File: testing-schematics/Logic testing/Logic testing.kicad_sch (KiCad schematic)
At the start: 14 parts, among them J1 Fencer's Wire, J2 Opponent's Wire, K1 G6K-2, K2 G6K-2, K3 G6K-2, Q1 BC547, Q2 BC547, Q3 BC547

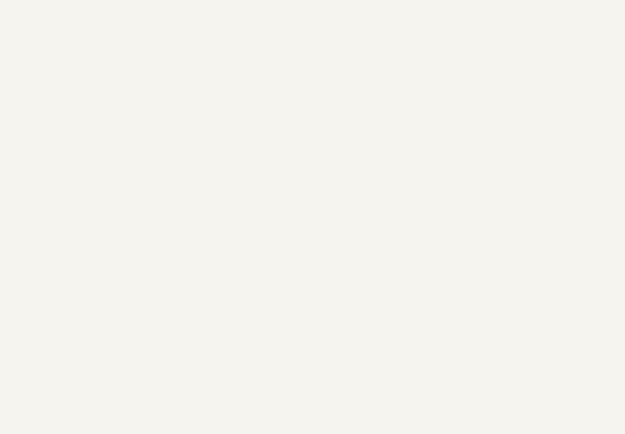
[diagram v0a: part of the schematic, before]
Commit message: Add voltage divider schematics and journal entry;
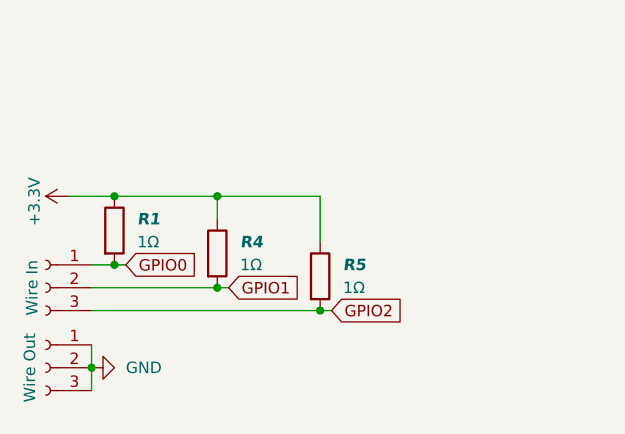
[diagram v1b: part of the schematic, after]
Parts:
- added J3: Wire In, symbol Connector:Conn_01x03_Socket
- added J4: Wire Out, symbol Connector:Conn_01x03_Socket
- added R1, R4, R5: 1Ω, symbol Device:R
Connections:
- net +3.3V: now also R1.1, R4.1, R5.1
- net GND: now also J4.1 (Pin_1), J4.2 (Pin_2), J4.3 (Pin_3)
- net GPIO1: now also J3.2 (Pin_2), R4.2
- net GPIO2: now also J3.3 (Pin_3), R5.2
- new net GPIO0: J3.1 (Pin_1), R1.2

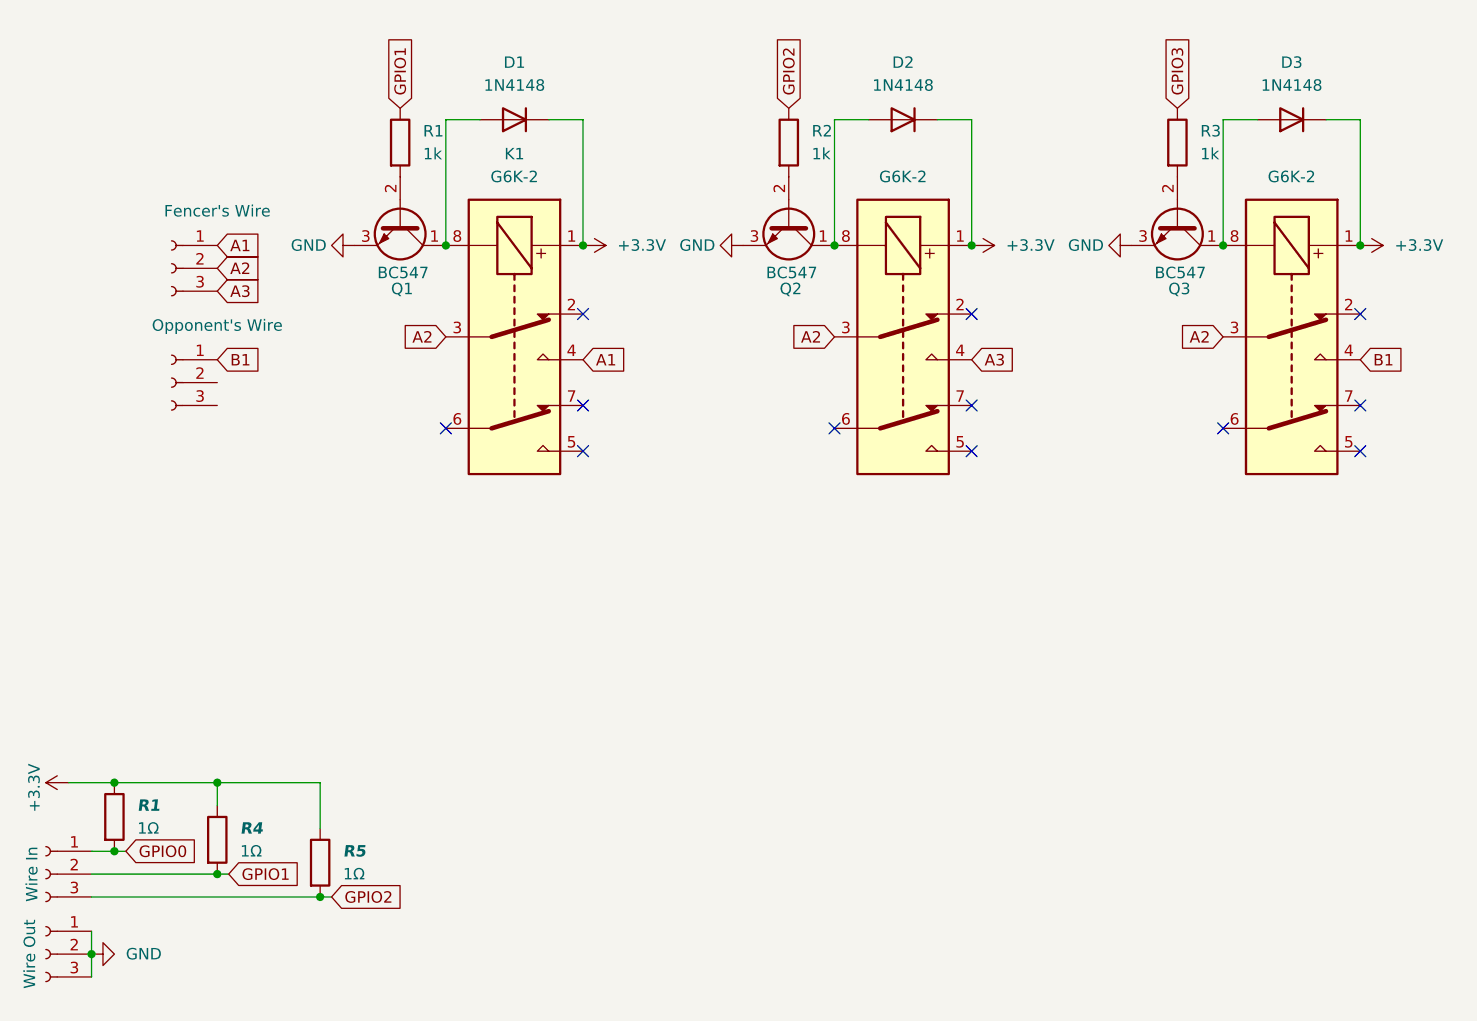
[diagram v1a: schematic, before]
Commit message: Add weapon tester & change layout
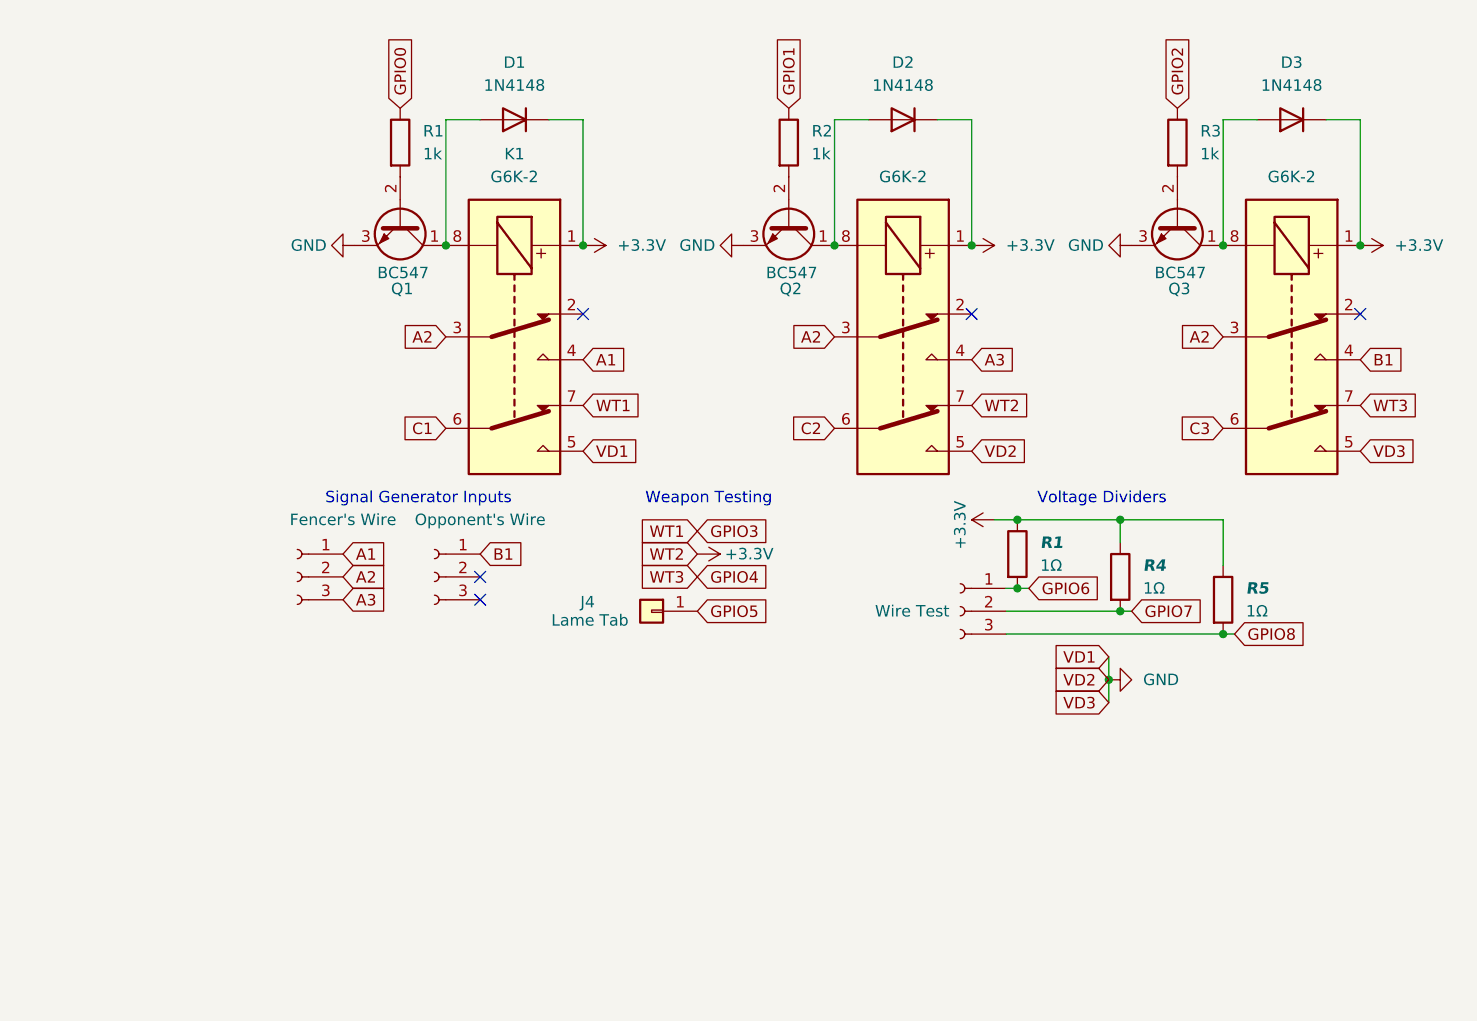
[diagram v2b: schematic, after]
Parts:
- removed J4: Wire Out, symbol Connector:Conn_01x03_Socket
- added J4: Lame Tab, symbol Connector_Generic:Conn_01x01
- J3: value Wire In -> Wire Test
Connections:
- net +3.3V: now also K2.7
- net GND: now also K1.5, K2.5, K3.5
- net GPIO0: now also R1.1; no longer J3.1 (Pin_1), R1.2
- net GPIO1: now also R2.1; no longer J3.2 (Pin_2), R1.1, R4.2
- net GPIO2: now also R3.1; no longer J3.3 (Pin_3), R2.1, R5.2
- net GPIO3: now also K1.7; no longer R3.1
- net C2: now reaches K2.6
- net C1: now reaches K1.6
- net C3: now reaches K3.6
- net GPIO4: now reaches K3.7
- new net GPIO5: J4.1 (Pin_1)
- new net GPIO6: J3.1 (Pin_1), R1.2
- new net GPIO7: J3.2 (Pin_2), R4.2
- new net GPIO8: J3.3 (Pin_3), R5.2
- no-connect marks 12 -> 5
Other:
- note added: "Signal Generator Inputs"
- note added: "Voltage Dividers"
- note added: "Weapon Testing"
- moved on the sheet: R1, R4, R5

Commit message: Update schematic and BOM
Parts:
- removed J3: Wire Test, symbol Connector:Conn_01x03_Socket
- added D4: 1N4148, Diode_THT:D_DO-35_SOD27_P7.62mm_Horizontal, symbol Diode:1N4148
- added J5: Test Output, symbol Connector:Conn_01x03_Socket
- added K4, K5: G6K-2, symbol Relay:G6K-2
- added Q4: BC547, Package_TO_SOT_THT:TO-92_Inline, symbol Transistor_BJT:BC547
- added R6: 1k, Resistor_THT:R_Axial_DIN0204_L3.6mm_D1.6mm_P7.62mm_Horizontal, symbol Device:R
- added U1: ESP32-S3, Package_DFN_QFN:QFN-56-1EP_7x7mm_P0.4mm_EP4x4mm, symbol MCU_Espressif:ESP32-S3
- J1: value Fencer's Wire -> External Box
- J2: value Opponent's Wire -> Aux Wire
- J4: footprint (none) -> Connector_Wire:SolderWire-0.5sqmm_1x01_D0.9mm_OD2.1mm
- R1, R2, R3, R4, R5: footprint (none) -> Resistor_THT:R_Axial_DIN0204_L3.6mm_D1.6mm_P7.62mm_Horizontal
- R7: renamed from R1; footprint (none) -> Resistor_THT:R_Axial_DIN0204_L3.6mm_D1.6mm_P7.62mm_Horizontal
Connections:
- net +3.3V: now also D4.1 (K), K4.1, K5.1
- net B1: now also K4.3; no longer K3.4
- net C1: now also J5.1 (Pin_1)
- net C2: now also J5.2 (Pin_2)
- net C3: now also J5.3 (Pin_3)
- net GND: now also Q4.3 (E), U1.57 (GND)
- net GPIO0: now also U1.5 (GPIO0)
- net GPIO1: now also U1.6 (GPIO1)
- net GPIO2: now also U1.7 (GPIO2)
- net GPIO3: now also U1.8 (GPIO3)
- net GPIO4: now also U1.9 (GPIO4)
- net GPIO5: now also U1.10 (GPIO5)
- net GPIO6: now also K4.2, U1.11 (GPIO6)
- net GPIO7: now also K4.7, U1.12 (GPIO7)
- net GPIO8: now also K5.2, U1.13 (GPIO8)
- net B2: now reaches J2.2 (Pin_2)
- net B2: now also K4.6
- net B3: now reaches J2.3 (Pin_3)
- net B3: now also K5.3
- new net: D4.2 (A), K4.8, K5.8, Q4.1 (C)
- new net: Q4.2 (B), R6.2
- new net: U1.2 (VDD3P3), U1.3 (VDD3P3)
- new net: U1.55 (VDDA), U1.56 (VDDA)
- new net GPIO9: R6.1, U1.14 (GPIO9)
- new net SG1: K3.4, K4.4
- no-connect marks 5 -> 52

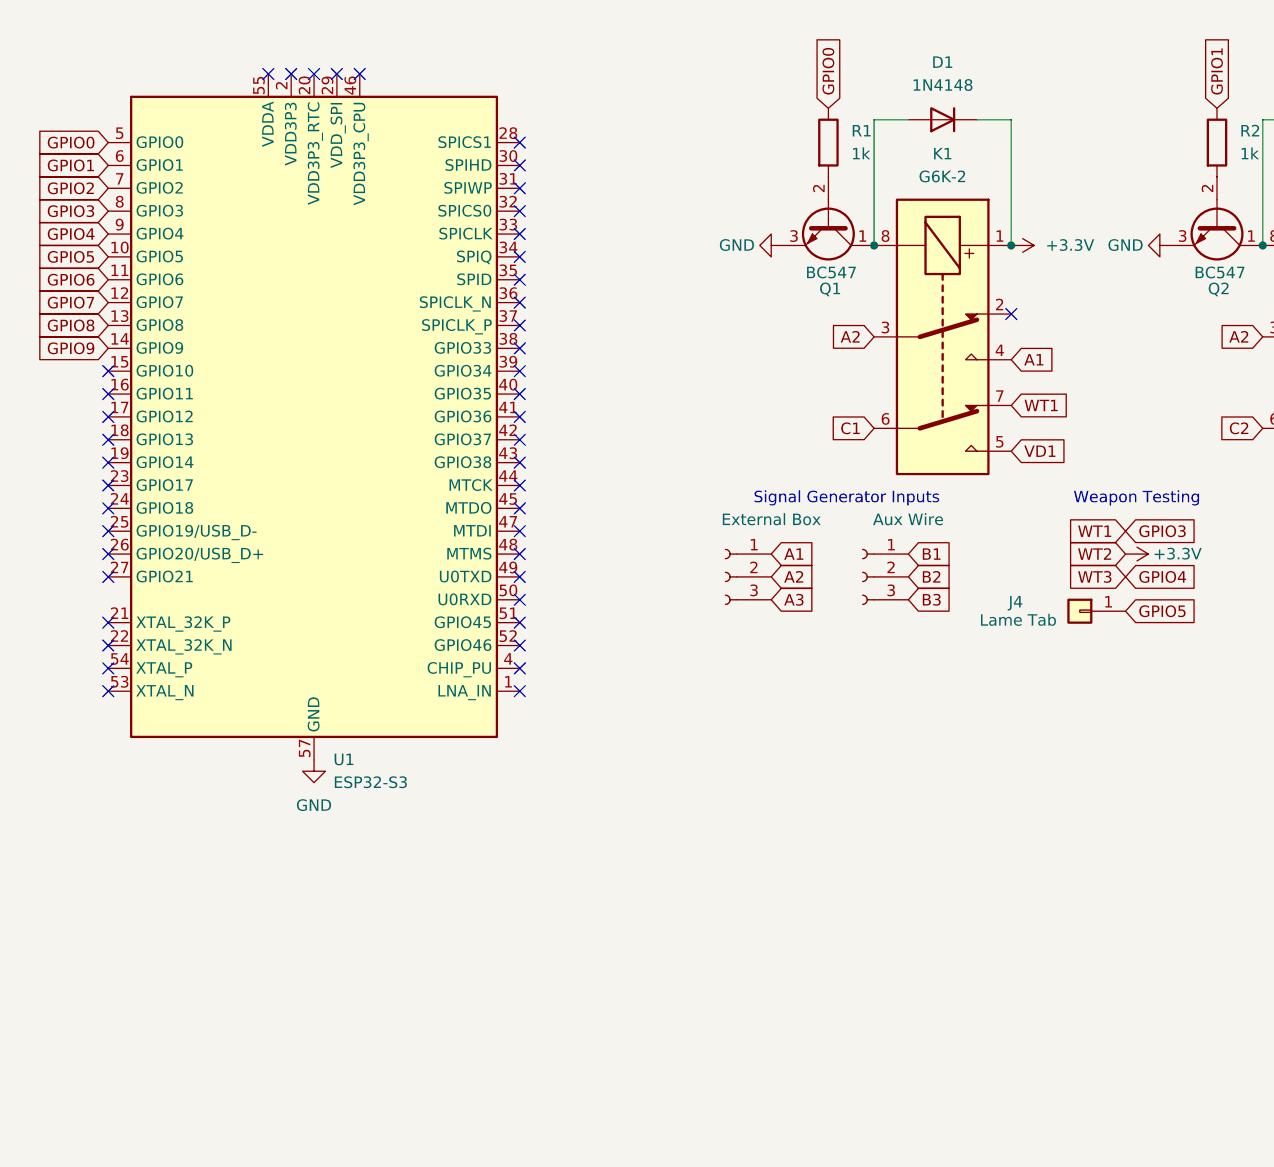
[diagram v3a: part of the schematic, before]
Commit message: Add usb, es32 c6, and voltage regulator
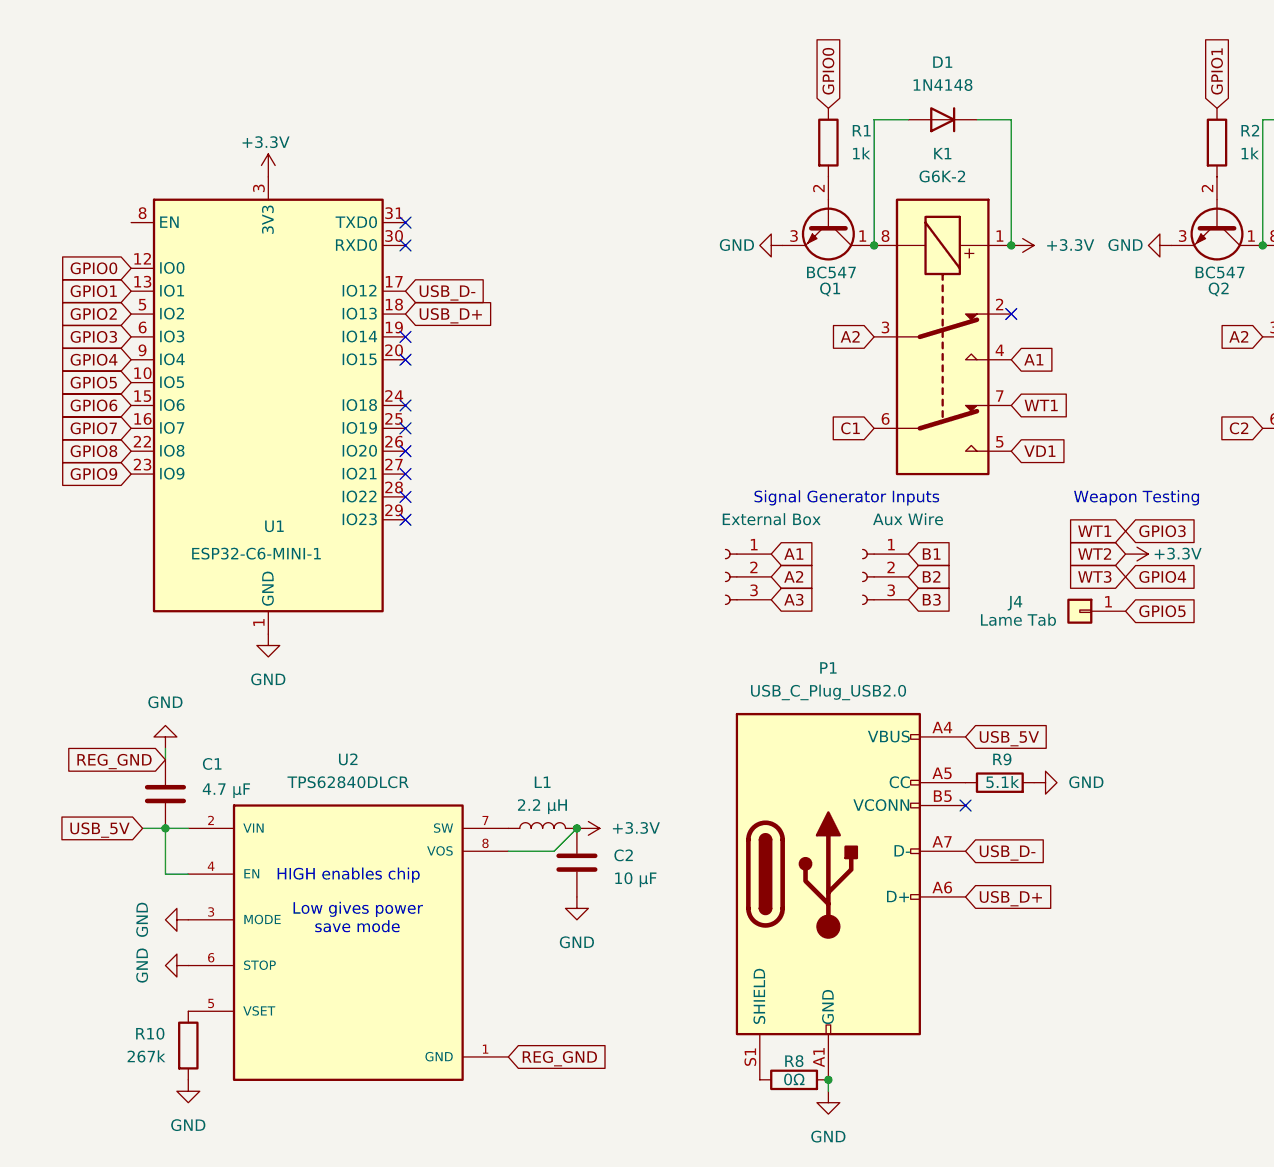
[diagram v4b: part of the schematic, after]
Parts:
- removed U1: ESP32-S3, Package_DFN_QFN:QFN-56-1EP_7x7mm_P0.4mm_EP4x4mm, symbol MCU_Espressif:ESP32-S3
- added C1: 4.7 µF, symbol Device:C
- added C2: 10 µF, symbol Device:C
- added L1: 2.2 µH, symbol Device:L
- added P1: USB_C_Plug_USB2.0, symbol Connector:USB_C_Plug_USB2.0
- added R10: 267k, symbol Device:R
- added R8: 0Ω, symbol Device:R
- added R9: 5.1k, symbol Device:R
- added U1: ESP32-C6-MINI-1, RF_Module:ESP32-C6-MINI-1, symbol RF_Module:ESP32-C6-MINI-1
- added U2: TPS62840DLCR, TPS62840DLCR:SON50P200X150X100-8N, symbol Imports:TPS62840DLCR
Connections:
- net +3.3V: now also C2.1, L1.2, U1.3 (3V3), U2.8 (VOS)
- net GND: now also C1.1, C2.2, P1.A1 (GND), P1.A12 (GND), P1.B1 (GND), P1.B12 (GND), R10.2, R8.2, R9.2, U1.1 (GND), U1.11 (GND), U1.14 (GND), U1.2 (GND), U1.36 (GND), U1.37 (GND), U1.38 (GND), U1.39 (GND), U1.40 (GND), U1.41 (GND), U1.42 (GND), U1.43 (GND), U1.44 (GND), U1.45 (GND), U1.46 (GND), U1.47 (GND), U1.48 (GND), U1.49 (GND), U1.50 (GND), U1.51 (GND), U1.52 (GND), U1.53 (GND), U2.1 (GND), U2.3 (MODE), U2.6 (STOP)
- net GPIO0: now also U1.12 (IO0)
- net GPIO1: now also U1.13 (IO1)
- net GPIO2: now also U1.5 (IO2)
- net GPIO3: now also U1.6 (IO3)
- net GPIO4: now also U1.9 (IO4)
- net GPIO5: now also U1.10 (IO5)
- net GPIO6: now also U1.15 (IO6)
- net GPIO7: now also U1.16 (IO7)
- net GPIO8: now also U1.22 (IO8)
- net GPIO9: now also U1.23 (IO9)
- new net: R10.1, U2.5 (VSET)
- new net: L1.1, U2.7 (SW)
- new net: P1.A5 (CC), R9.1
- new net: P1.S1 (SHIELD), R8.1
- new net USB_5V: C1.2, P1.A4 (VBUS), P1.A9 (VBUS), P1.B4 (VBUS), P1.B9 (VBUS), U2.2 (VIN), U2.4 (EN)
- new net USB_D+: P1.A6 (D+), U1.18 (IO13)
- new net USB_D-: P1.A7 (D-), U1.17 (IO12)
- no-connect marks 52 -> 19
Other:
- note added: "HIGH enables chip"
- note added: "Low gives power save mode"

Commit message: Transitioned relays to 5V; Fixed USB port shield; Added buttons, switches;
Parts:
- added C3: 1 nF, symbol Device:C
- added R11: 1M, symbol Device:R
- added R12, R13, R14, R15: 10k, symbol Device:R
- added SW1: SW_SPDT, symbol Switch:SW_SPDT
- added SW2: SW_DP3T, symbol Switch:SW_DP3T
- added SW3: SW_Push, symbol Switch:SW_Push
- R1, R2, R3, R6: value 1k -> 500
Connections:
- net +3.3V: now also R12.2, SW2.3, SW3.1; no longer D1.1 (K), D2.1 (K), D3.1 (K), D4.1 (K), K1.1, K2.1, K3.1, K4.1, K5.1
- net GND: now also R13.2, R14.1, R15.1, SW1.1 (A)
- net WPS A: now reaches U1.19 (IO14)
- net WPS A: now also R13.1, SW2.1
- net WPS B: now reaches U1.20 (IO15)
- net WPS B: now also R14.2, SW2.4
- net VDR1: now reaches U1.24 (IO18)
- net VDR1: now also K4.2, R7.2
- net VDR2: now reaches U1.25 (IO19)
- net VDR2: now also K4.7, R4.2
- net VDR3: now reaches U1.26 (IO20)
- net VDR3: now also K5.2, R5.2
- net at U1.8 (EN): now also SW1.2 (B)
- net at P1.S1 (SHIELD): now also C3.1, R11.1; no longer R8.1
- net GPIO0 renamed REL1
- net GPIO1 renamed REL2
- net GPIO2 renamed REL3
- net GPIO3 renamed REL4
- net REL4: now also R6.1; no longer K1.7
- net GPIO4 renamed LAME
- net LAME: now also J4.1 (Pin_1); no longer K3.7
- net GPIO5 renamed BTN USE
- net BTN USE: now also R15.2, SW3.2; no longer J4.1 (Pin_1)
- removed net GPIO6: K4.2, R7.2, U1.15 (IO6)
- removed net GPIO7: K4.7, R4.2, U1.16 (IO7)
- removed net GPIO8: K5.2, R5.2, U1.22 (IO8)
- net GPIO9 renamed WT3
- net WT3: now also K3.7; no longer R6.1
- net USB_5V renamed +5V
- net +5V: now also D1.1 (K), D2.1 (K), D3.1 (K), D4.1 (K), K1.1, K2.1, K3.1, K4.1, K5.1
- new net: C3.2, R11.2, R8.1
- new net: R12.1, SW1.3 (C)
- new net SCL: U1.16 (IO7)
- new net SDA: U1.15 (IO6)
- new net WT1: K1.7, U1.22 (IO8)
- no-connect marks 19 -> 15
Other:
- moved on the sheet: R8
